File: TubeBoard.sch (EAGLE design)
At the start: 4 parts, among them IC1 74141N, IC2 74141N

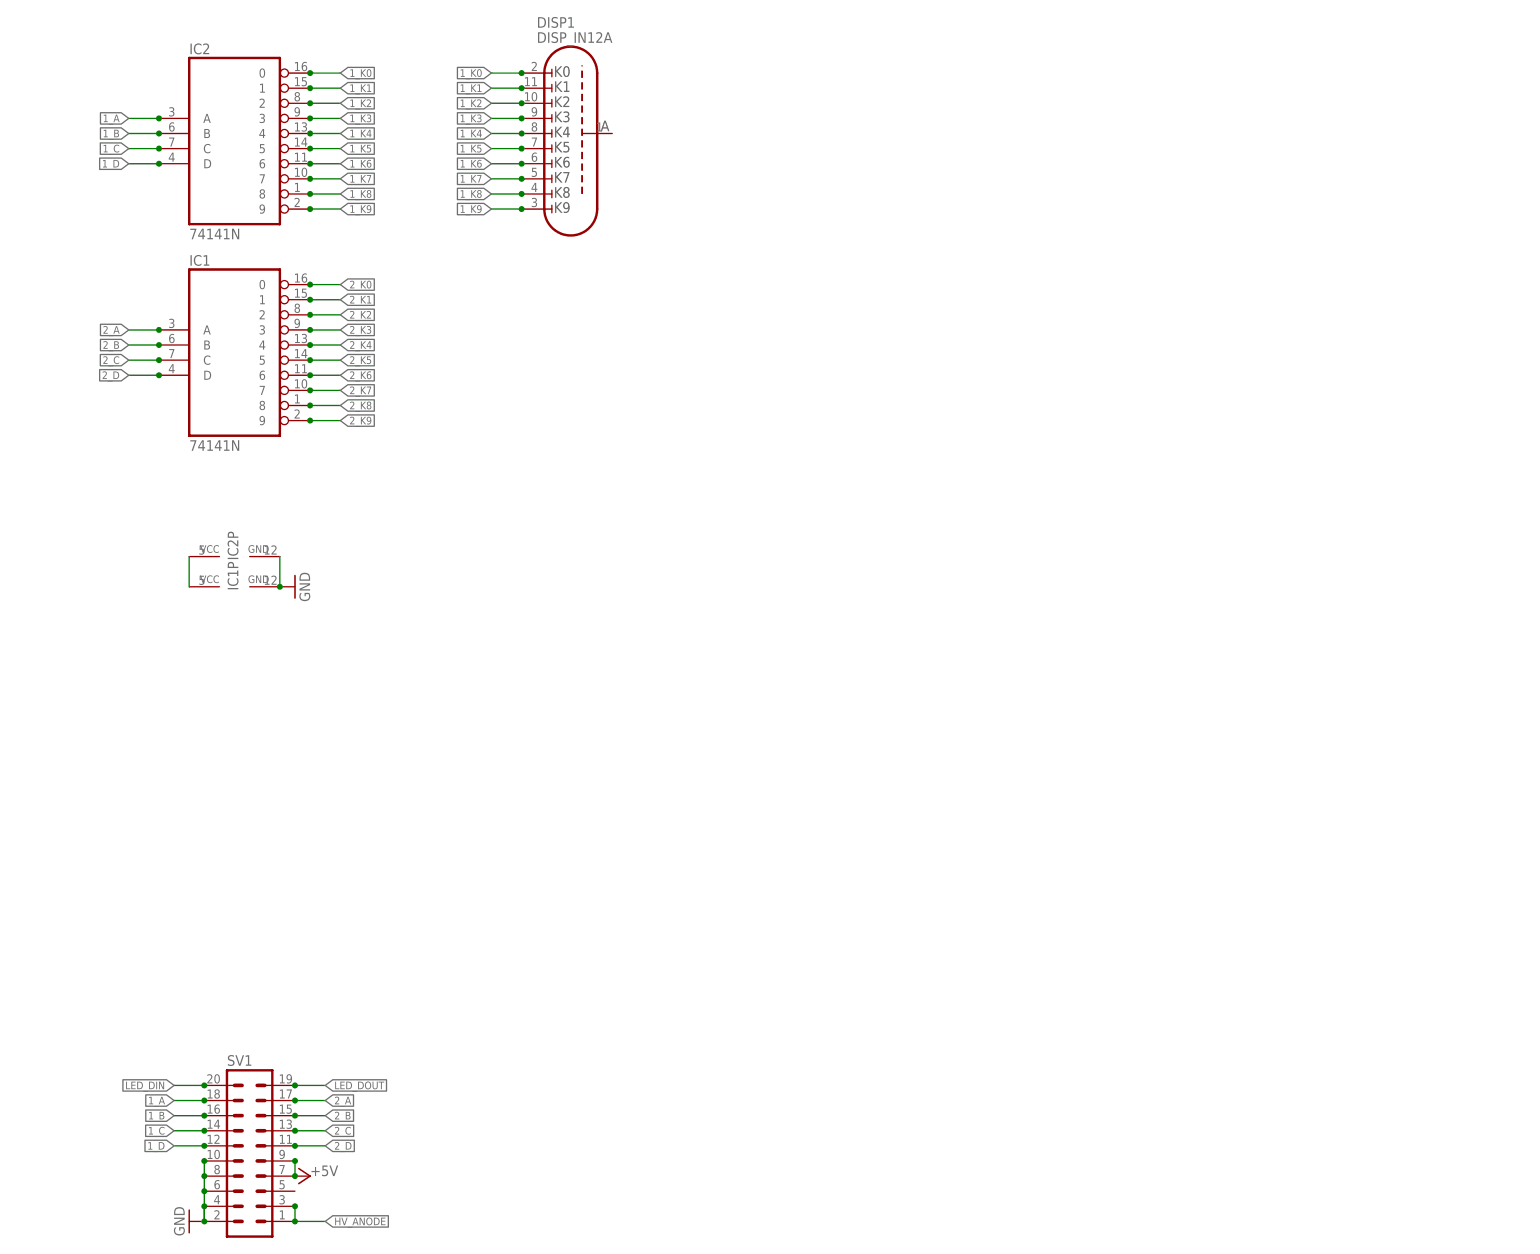
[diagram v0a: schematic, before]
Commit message: added shift register-based nixie driver
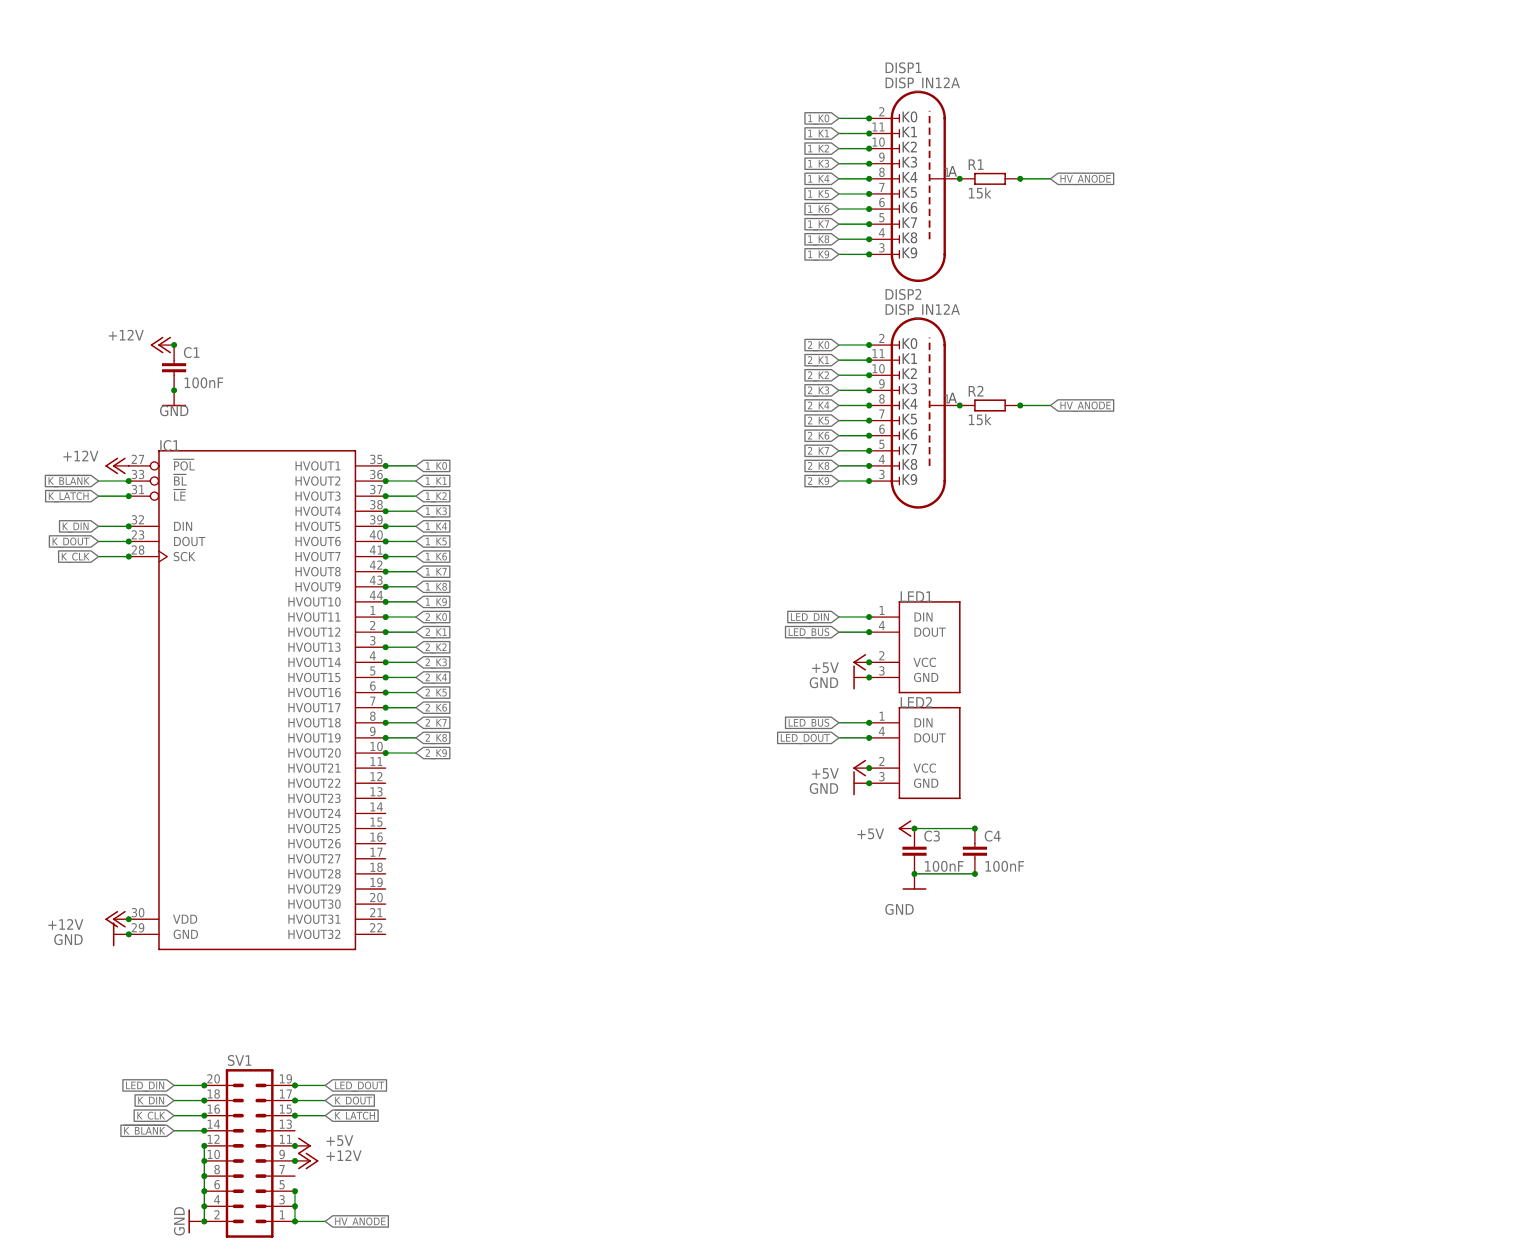
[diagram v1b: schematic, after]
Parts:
- removed IC2: 74141N, 74xx-eu:74141N
- added C1, C3, C4: 100nF, rcl:C-EUC1206
- added DISP2: DISP_IN12A, dp_devices:DISP_IN12A
- added LED1, LED2: (no value), Parts:NEOPIXEL-5MMLED-4PIN
- added R1, R2: 15k, rcl:R-EU_0411/12
- IC1: value 74141N -> HV5530PQFP-44; device 74xx-eu:74141N -> Parts:HV5530PQFP-44
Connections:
- removed net 1_A: IC2A.A, SV1.18
- removed net 1_B: IC2A.B, SV1.16
- removed net 1_C: IC2A.C, SV1.14
- removed net 1_D: IC2A.D, SV1.12
- removed net 2_A: IC1A.A, SV1.17
- removed net 2_B: IC1A.B, SV1.15
- removed net 2_C: IC1A.C, SV1.13
- removed net 2_D: IC1A.D, SV1.11
- new net !K_BLANK: IC1.!BL, SV1.14
- new net !K_LATCH: IC1.!LE, SV1.15
- new net +12V: C1.1, IC1.!POL, IC1.VDD, SV1.9
- new net K_CLK: IC1.SCK, SV1.16
- new net K_DIN: IC1.DIN, SV1.18
- new net K_DOUT: IC1.DOUT, SV1.17
- new net LED_BUS: LED1.DOUT, LED2.DIN
- new net N$1: DISP1.ANODE, R1.1
- net +5V: now also C3.1, C4.1, LED1.VCC, LED2.VCC, SV1.11; no longer SV1.7, SV1.9
- net 1_K0: now also IC1.HVOUT1; no longer IC2A.0
- net 1_K1: now also IC1.HVOUT2; no longer IC2A.1
- net 1_K2: now also IC1.HVOUT3; no longer IC2A.2
- net 1_K3: now also IC1.HVOUT4; no longer IC2A.3
- net 1_K4: now also IC1.HVOUT5; no longer IC2A.4
- net 1_K5: now also IC1.HVOUT6; no longer IC2A.5
- net 1_K6: now also IC1.HVOUT7; no longer IC2A.6
- net 1_K7: now also IC1.HVOUT8; no longer IC2A.7
- net 1_K8: now also IC1.HVOUT9; no longer IC2A.8
- net 1_K9: now also IC1.HVOUT10; no longer IC2A.9
- net 2_K0: now also DISP2.K0, IC1.HVOUT11; no longer IC1A.0
- net 2_K1: now also DISP2.K1, IC1.HVOUT12; no longer IC1A.1
- net 2_K2: now also DISP2.K2, IC1.HVOUT13; no longer IC1A.2
- net 2_K3: now also DISP2.K3, IC1.HVOUT14; no longer IC1A.3
- net 2_K4: now also DISP2.K4, IC1.HVOUT15; no longer IC1A.4
- net 2_K5: now also DISP2.K5, IC1.HVOUT16; no longer IC1A.5
- net 2_K6: now also DISP2.K6, IC1.HVOUT17; no longer IC1A.6
- net 2_K7: now also DISP2.K7, IC1.HVOUT18; no longer IC1A.7
- net 2_K8: now also DISP2.K8, IC1.HVOUT19; no longer IC1A.8
- net 2_K9: now also DISP2.K9, IC1.HVOUT20; no longer IC1A.9
- net GND: now also C1.2, C3.2, C4.2, IC1.GND, LED1.GND, LED2.GND, SV1.12; no longer IC1P.GND, IC2P.GND
- net HV_ANODE: now also R1.2, R2.2, SV1.5
- net LED_DIN: now also LED1.DIN
- net LED_DOUT: now also LED2.DOUT
- net N$2: now also DISP2.ANODE, R2.1; no longer IC1P.VCC, IC2P.VCC
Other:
- moved on the sheet: DISP1

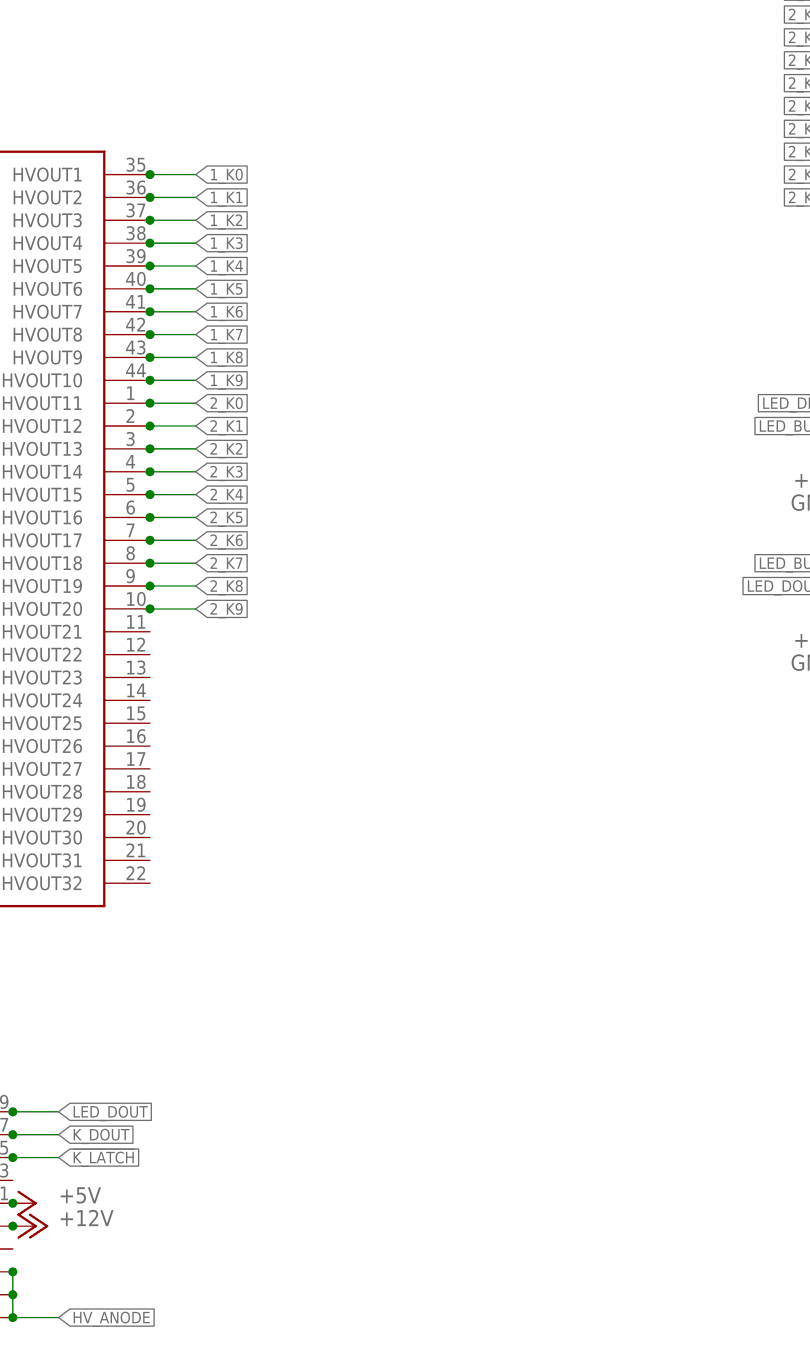
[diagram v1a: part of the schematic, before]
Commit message: Finished routing tube board
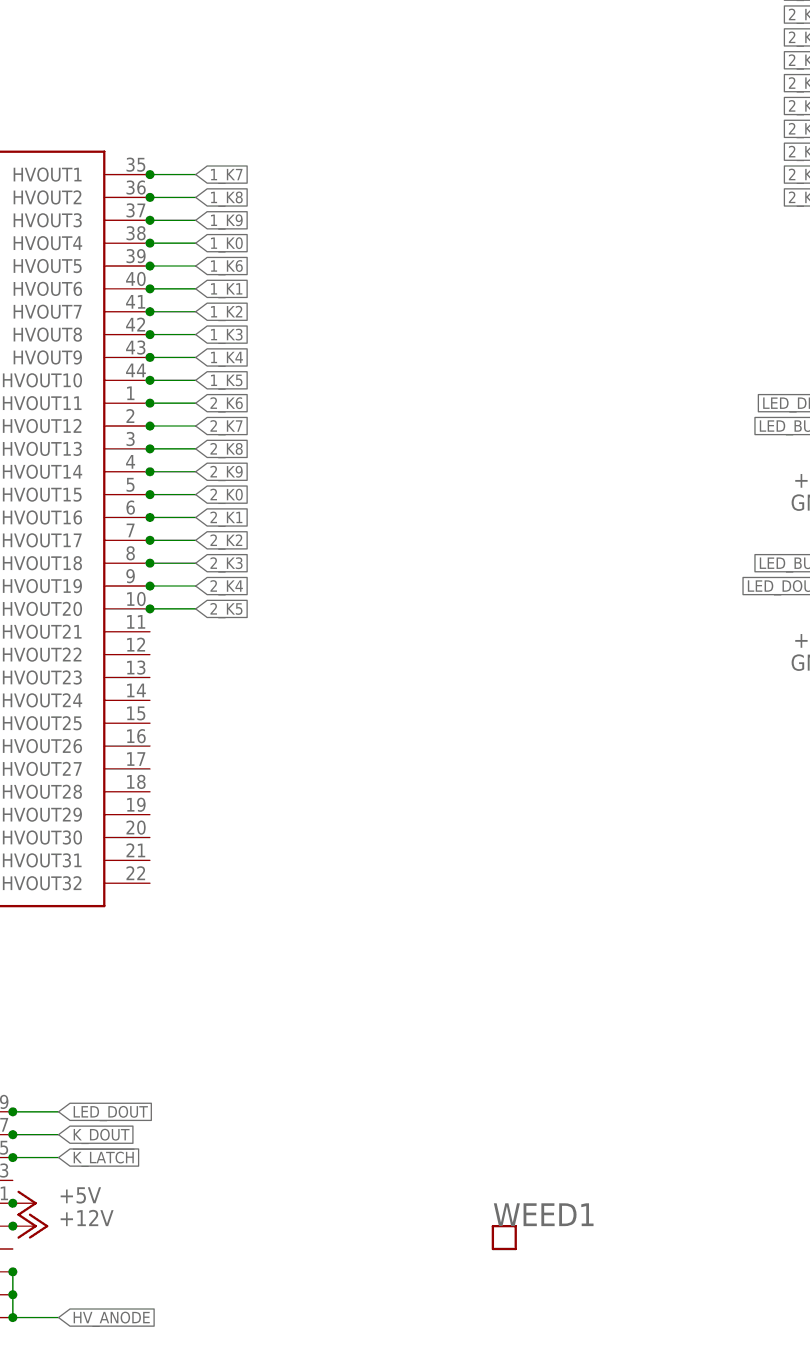
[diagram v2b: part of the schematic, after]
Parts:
- added WEED1: WEED, Parts:WEED
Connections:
- net 1_K0: now also IC1.HVOUT4; no longer IC1.HVOUT1
- net 1_K1: now also IC1.HVOUT6; no longer IC1.HVOUT2
- net 1_K2: now also IC1.HVOUT7; no longer IC1.HVOUT3
- net 1_K3: now also IC1.HVOUT8; no longer IC1.HVOUT4
- net 1_K4: now also IC1.HVOUT9; no longer IC1.HVOUT5
- net 1_K5: now also IC1.HVOUT10; no longer IC1.HVOUT6
- net 1_K6: now also IC1.HVOUT5; no longer IC1.HVOUT7
- net 1_K7: now also IC1.HVOUT1; no longer IC1.HVOUT8
- net 1_K8: now also IC1.HVOUT2; no longer IC1.HVOUT9
- net 1_K9: now also IC1.HVOUT3; no longer IC1.HVOUT10
- net 2_K0: now also IC1.HVOUT15; no longer IC1.HVOUT11
- net 2_K1: now also IC1.HVOUT16; no longer IC1.HVOUT12
- net 2_K2: now also IC1.HVOUT17; no longer IC1.HVOUT13
- net 2_K3: now also IC1.HVOUT18; no longer IC1.HVOUT14
- net 2_K4: now also IC1.HVOUT19; no longer IC1.HVOUT15
- net 2_K5: now also IC1.HVOUT20; no longer IC1.HVOUT16
- net 2_K6: now also IC1.HVOUT11; no longer IC1.HVOUT17
- net 2_K7: now also IC1.HVOUT12; no longer IC1.HVOUT18
- net 2_K8: now also IC1.HVOUT13; no longer IC1.HVOUT19
- net 2_K9: now also IC1.HVOUT14; no longer IC1.HVOUT20
